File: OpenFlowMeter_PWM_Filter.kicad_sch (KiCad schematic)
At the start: 10 parts, among them U3 LT1492

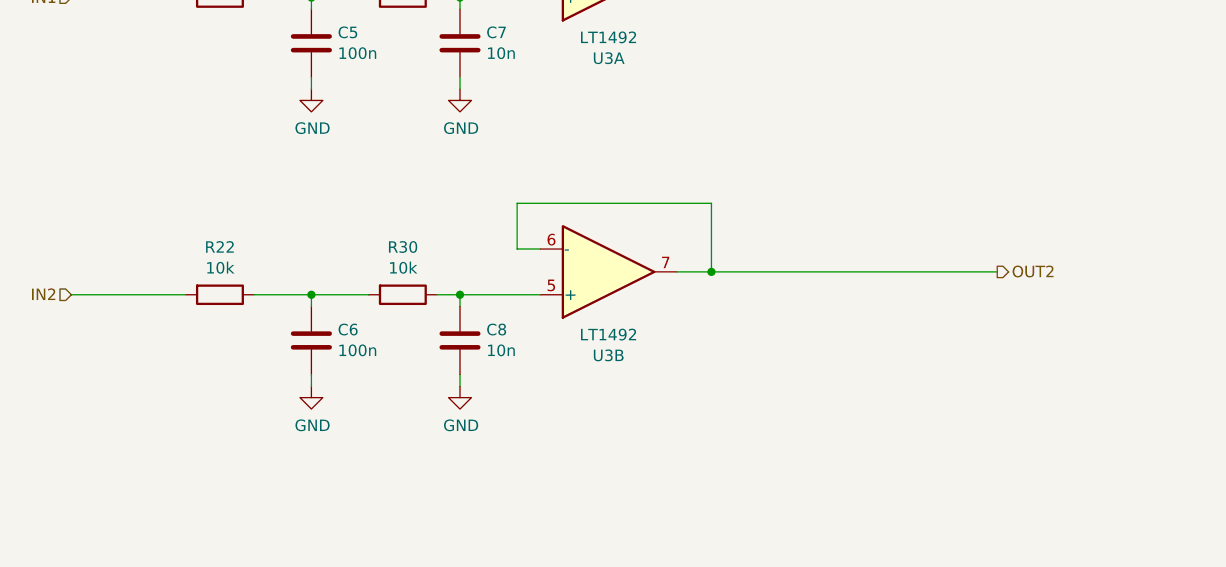
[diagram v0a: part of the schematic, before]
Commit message: fixed input / output numbering
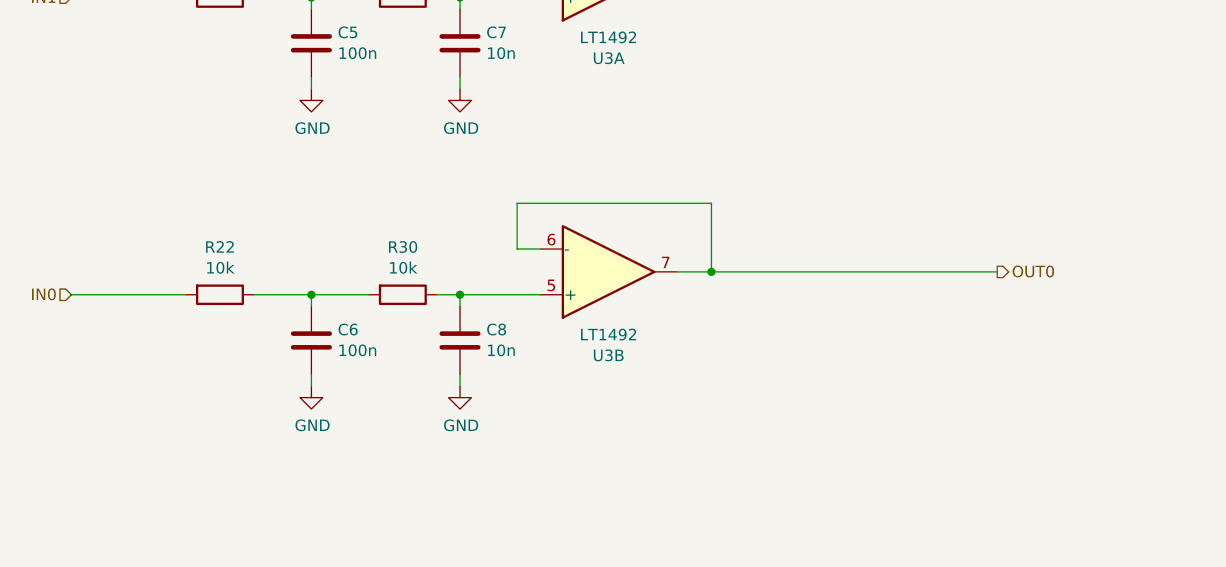
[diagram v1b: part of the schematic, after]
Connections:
- net IN2 renamed IN0
- net OUT2 renamed OUT0
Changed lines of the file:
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@@
     (effects (font (size 2.4892 2.4892) (thickness 0.4978) bold) (justify left bottom))
   )
-  (hierarchical_label "IN2" (shape input) (at 87.63 127 180) (fields_autoplaced)
+  (hierarchical_label "IN1" (shape input) (at 87.63 93.98 180) (fields_autoplaced)
     (effects (font (size 1.27 1.27)) (justify right))
-  )
-  (hierarchical_label "OUT2" (shape output) (at 190.5 124.46 0) (fields_autoplaced)
-    (effects (font (size 1.27 1.27)) (justify left))
   )
   (hierarchical_label "OUT1" (shape output) (at 190.5 91.44 0) (fields_autoplaced)
     (effects (font (size 1.27 1.27)) (justify left))
   )
-  (hierarchical_label "IN1" (shape input) (at 87.63 93.98 180) (fields_autoplaced)
+  (hierarchical_label "OUT0" (shape output) (at 190.5 124.46 0) (fields_autoplaced)
+    (effects (font (size 1.27 1.27)) (justify left))
+  )
+  (hierarchical_label "IN0" (shape input) (at 87.63 127 180) (fields_autoplaced)
     (effects (font (size 1.27 1.27)) (justify right))
   )
@@
           (reference "U3") (unit 1)
         )
+        (path "/25e5aa8e-2696-44a3-8d3c-c2c53f2923cf/100f98e3-4296-40f9-94c5-6b164cc256aa"
+          (reference "U11") (unit 1)
+        )
       )
     )
@@
           (reference "U3") (unit 3)
         )
+        (path "/25e5aa8e-2696-44a3-8d3c-c2c53f2923cf/100f98e3-4296-40f9-94c5-6b164cc256aa"
+          (reference "U11") (unit 3)
+        )
       )
     )
@@
           (reference "#PWR017") (unit 1)
         )
+        (path "/25e5aa8e-2696-44a3-8d3c-c2c53f2923cf/100f98e3-4296-40f9-94c5-6b164cc256aa"
+          (reference "#PWR095") (unit 1)
+        )
       )
     )
@@
           (reference "C9") (unit 1)
         )
+        (path "/25e5aa8e-2696-44a3-8d3c-c2c53f2923cf/100f98e3-4296-40f9-94c5-6b164cc256aa"
+          (reference "C38") (unit 1)
+        )
       )
     )
@@
         (path "/25e5aa8e-2696-44a3-8d3c-c2c53f2923cf/00000000-0000-0000-0000-000061b7a600"
           (reference "#PWR018") (unit 1)
+        )
+        (path "/25e5aa8e-2696-44a3-8d3c-c2c53f2923cf/100f98e3-4296-40f9-94c5-6b164cc256aa"
+          (reference "#PWR097") (unit 1)
         )
       )
@@
           (reference "U3") (unit 2)
         )
+        (path "/25e5aa8e-2696-44a3-8d3c-c2c53f2923cf/100f98e3-4296-40f9-94c5-6b164cc256aa"
+          (reference "U11") (unit 2)
+        )
       )
     )
@@
           (reference "R8") (unit 1)
         )
+        (path "/25e5aa8e-2696-44a3-8d3c-c2c53f2923cf/100f98e3-4296-40f9-94c5-6b164cc256aa"
+          (reference "R62") (unit 1)
+        )
       )
     )
@@
           (reference "R29") (unit 1)
         )
+        (path "/25e5aa8e-2696-44a3-8d3c-c2c53f2923cf/100f98e3-4296-40f9-94c5-6b164cc256aa"
+          (reference "R64") (unit 1)
+        )
       )
     )
@@
           (reference "C5") (unit 1)
         )
+        (path "/25e5aa8e-2696-44a3-8d3c-c2c53f2923cf/100f98e3-4296-40f9-94c5-6b164cc256aa"
+          (reference "C34") (unit 1)
+        )
       )
     )
@@
           (reference "C7") (unit 1)
         )
+        (path "/25e5aa8e-2696-44a3-8d3c-c2c53f2923cf/100f98e3-4296-40f9-94c5-6b164cc256aa"
+          (reference "C36") (unit 1)
+        )
       )
     )
@@
           (reference "#PWR09") (unit 1)
         )
+        (path "/25e5aa8e-2696-44a3-8d3c-c2c53f2923cf/100f98e3-4296-40f9-94c5-6b164cc256aa"
+          (reference "#PWR092") (unit 1)
+        )
       )
     )
@@
           (reference "#PWR01") (unit 1)
         )
+        (path "/25e5aa8e-2696-44a3-8d3c-c2c53f2923cf/100f98e3-4296-40f9-94c5-6b164cc256aa"
+          (reference "#PWR090") (unit 1)
+        )
       )
     )
@@
           (reference "R22") (unit 1)
         )
+        (path "/25e5aa8e-2696-44a3-8d3c-c2c53f2923cf/100f98e3-4296-40f9-94c5-6b164cc256aa"
+          (reference "R63") (unit 1)
+        )
       )
     )
@@
           (reference "R30") (unit 1)
         )
+        (path "/25e5aa8e-2696-44a3-8d3c-c2c53f2923cf/100f98e3-4296-40f9-94c5-6b164cc256aa"
+          (reference "R65") (unit 1)
+        )
       )
     )
@@
           (reference "C6") (unit 1)
         )
+        (path "/25e5aa8e-2696-44a3-8d3c-c2c53f2923cf/100f98e3-4296-40f9-94c5-6b164cc256aa"
+          (reference "C35") (unit 1)
+        )
       )
     )
@@
           (reference "C8") (unit 1)
         )
+        (path "/25e5aa8e-2696-44a3-8d3c-c2c53f2923cf/100f98e3-4296-40f9-94c5-6b164cc256aa"
+          (reference "C37") (unit 1)
+        )
       )
     )
@@
           (reference "#PWR010") (unit 1)
         )
+        (path "/25e5aa8e-2696-44a3-8d3c-c2c53f2923cf/100f98e3-4296-40f9-94c5-6b164cc256aa"
+          (reference "#PWR093") (unit 1)
+        )
       )
     )
@@
           (reference "#PWR08") (unit 1)
         )
+        (path "/25e5aa8e-2696-44a3-8d3c-c2c53f2923cf/100f98e3-4296-40f9-94c5-6b164cc256aa"
+          (reference "#PWR091") (unit 1)
+        )
       )
     )
@@
           (reference "#PWR019") (unit 1)
         )
+        (path "/25e5aa8e-2696-44a3-8d3c-c2c53f2923cf/100f98e3-4296-40f9-94c5-6b164cc256aa"
+          (reference "#PWR094") (unit 1)
+        )
       )
     )
@@
           (reference "#PWR020") (unit 1)
         )
-      )
+        (path "/25e5aa8e-2696-44a3-8d3c-c2c53f2923cf/100f98e3-4296-40f9-94c5-6b164cc256aa"
+          (reference "#PWR096") (unit 1)
+        )
+      )
